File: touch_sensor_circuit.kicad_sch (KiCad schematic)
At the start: 6 parts, among them J2 Conn_01x04_Pin, U2 SN74LVC1G14DBV

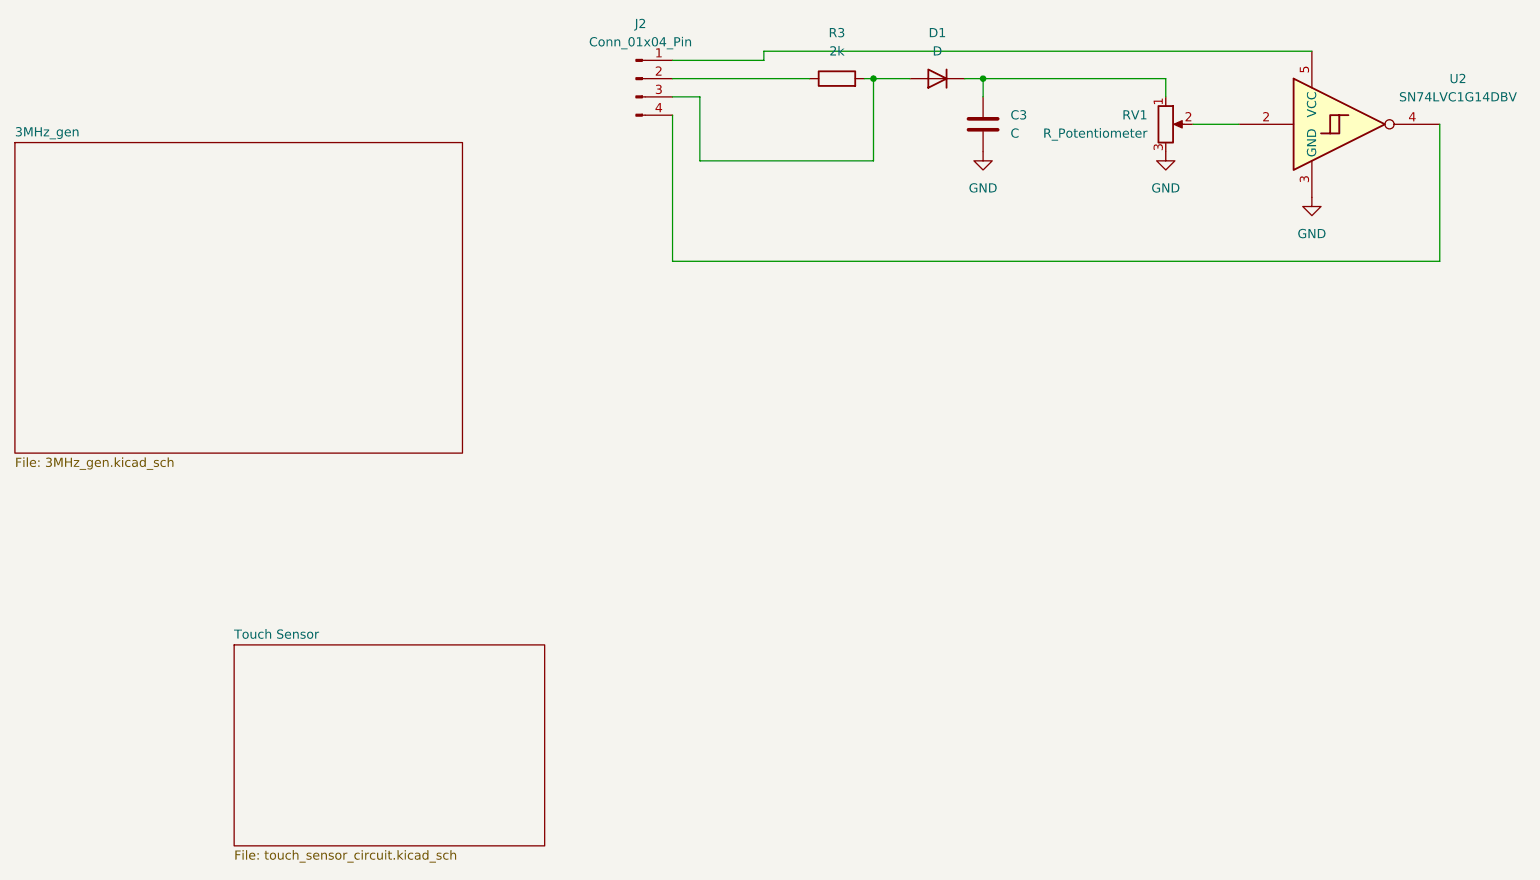
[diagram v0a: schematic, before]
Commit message: changed schematic hierarchy
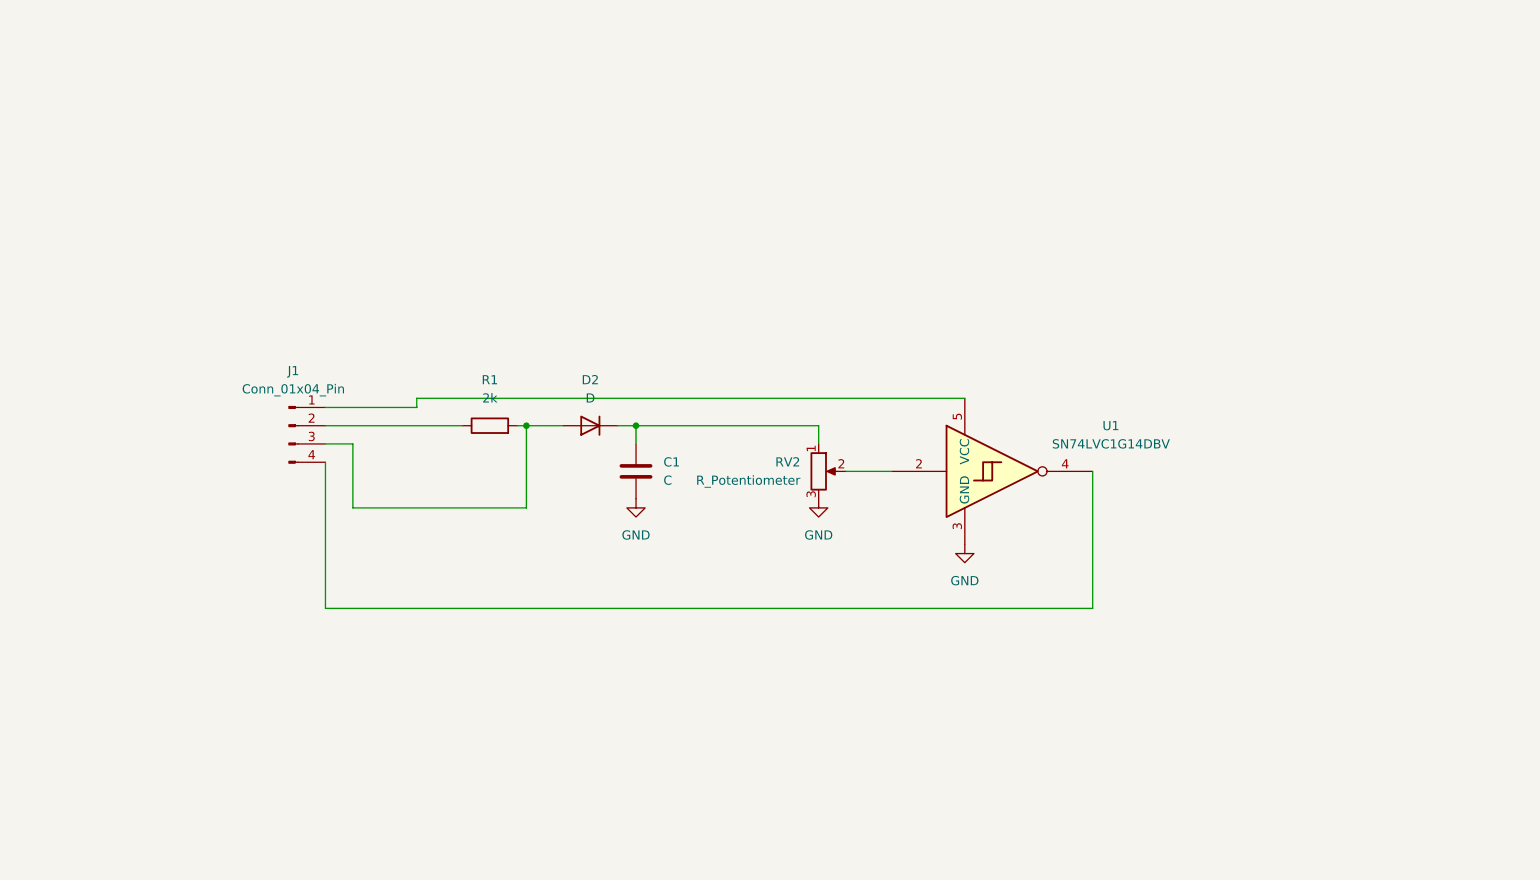
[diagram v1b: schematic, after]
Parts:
- removed C3: C, symbol Device:C
- removed D1: D, symbol Device:D
- removed J2: Conn_01x04_Pin, Connector_Wire:SolderWire-1.5sqmm_1x04_P6mm_D1.7mm_OD3mm, symbol Connector:Conn_01x04_Pin
- removed R3: 2k, symbol Device:R
- removed RV1: R_Potentiometer, symbol Device:R_Potentiometer
- removed U2: SN74LVC1G14DBV, Package_TO_SOT_SMD:SOT-23-5, symbol 74xGxx:SN74LVC1G14DBV
- added C1: C, symbol Device:C
- added D2: D, symbol Device:D
- added J1: Conn_01x04_Pin, Connector_Wire:SolderWire-1.5sqmm_1x04_P6mm_D1.7mm_OD3mm, symbol Connector:Conn_01x04_Pin
- added R1: 2k, symbol Device:R
- added RV2: R_Potentiometer, symbol Device:R_Potentiometer
- added U1: SN74LVC1G14DBV, Package_TO_SOT_SMD:SOT-23-5, symbol 74xGxx:SN74LVC1G14DBV
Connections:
- net GND: now also C1.2, RV2.3, U1.3 (GND)
- new net: J1.1 (Pin_1), U1.5 (VCC)
- new net: J1.2 (Pin_2), R1.1
- new net: D2.2 (A), J1.3 (Pin_3), R1.2
- new net: J1.4 (Pin_4), U1.4
- new net: C1.1, D2.1 (K), RV2.1
- new net: RV2.2, U1.2
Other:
- removed sheet 3MHz_gen
- removed sheet Touch Sensor
- title: Root -> (none)
